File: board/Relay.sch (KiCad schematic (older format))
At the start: 18 parts, among them K1 JS1-12V-F, K2 JS1-12V-F, K3 JS1-12V-F, K4 JS1-12V-F, U4 ULN2003A

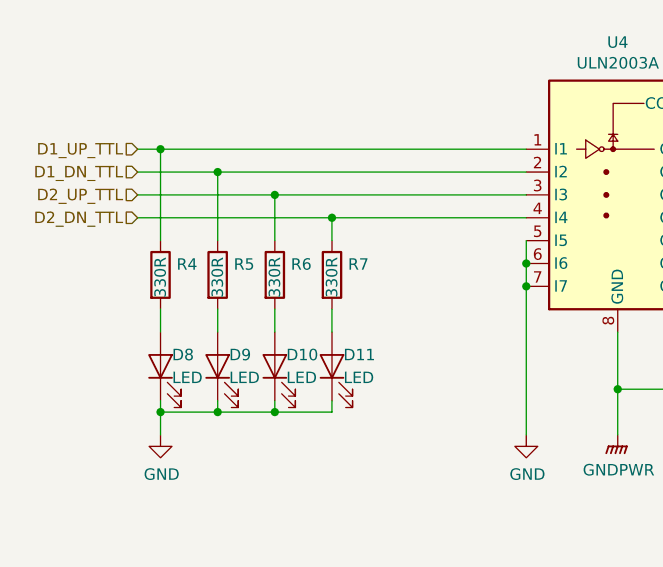
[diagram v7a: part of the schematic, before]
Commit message: Update all footprints to KiCad 5 paths
* All footprints updated.
* 3D models for the relays seem to be missing from KiCad, however, so I
  have a copy in my personal library. Mostly cosmetic.
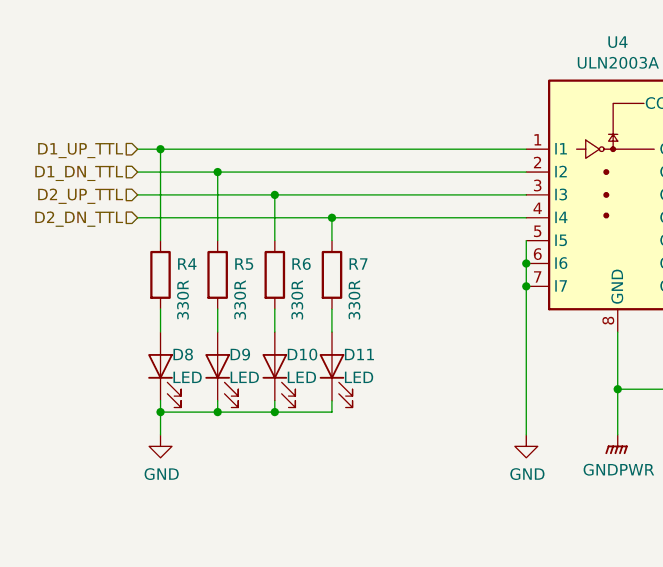
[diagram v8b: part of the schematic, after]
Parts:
- C13: footprint Capacitors_THT:C_Disc_D5.0mm_W2.5mm_P2.50mm -> Capacitor_THT:C_Disc_D5.0mm_W2.5mm_P2.50mm
- D1, D2, D3, D4: footprint Diodes_THT:D_DO-41_SOD81_P10.16mm_Horizontal -> Diode_THT:D_DO-41_SOD81_P10.16mm_Horizontal
- D10, D11, D8, D9: footprint LEDs:LED_D3.0mm -> LED_THT:LED_D3.0mm
- K1, K2, K3, K4: footprint Relays_THT:Relay_SPDT_SANYOU_SRD_Series_Form_C -> Relay_THT:Relay_SPDT_SANYOU_SRD_Series_Form_C
- R4, R5, R6, R7: footprint Resistors_THT:R_Axial_DIN0207_L6.3mm_D2.5mm_P10.16mm_Horizontal -> Resistor_THT:R_Axial_DIN0207_L6.3mm_D2.5mm_P10.16mm_Horizontal
- U4: footprint Housings_DIP:DIP-16_W7.62mm_LongPads -> Package_DIP:DIP-16_W7.62mm_LongPads
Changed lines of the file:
@@
 F 0 "U4" H 3150 3367 50  0000 C CNN
 F 1 "ULN2003A" H 3150 3276 50  0000 C CNN
-F 2 "Housings_DIP:DIP-16_W7.62mm_LongPads" H 3200 2150 50  0001 L CNN
+F 2 "Package_DIP:DIP-16_W7.62mm_LongPads" H 3200 2150 50  0001 L CNN
 F 3 "http://www.ti.com/lit/ds/symlink/uln2003a.pdf" H 3250 2500 50  0001 C CNN
 	1    3150 2700
@@
 F 0 "K1" H 6880 2096 50  0000 L CNN
 F 1 "JS1-12V-F" H 6880 2005 50  0000 L CNN
-F 2 "Relays_THT:Relay_SPDT_SANYOU_SRD_Series_Form_C" H 6900 2000 50  0001 L CNN
+F 2 "Relay_THT:Relay_SPDT_SANYOU_SRD_Series_Form_C" H 6900 2000 50  0001 L CNN
 F 3 "https://www3.panasonic.biz/ac/cdn/e/control/relay/power/catalog/mech_eng_js.pdf" H 6450 2050 50  0001 C CNN
 	1    6450 2050
@@
 F 0 "K2" H 6880 3046 50  0000 L CNN
 F 1 "JS1-12V-F" H 6880 2955 50  0000 L CNN
-F 2 "Relays_THT:Relay_SPDT_SANYOU_SRD_Series_Form_C" H 6900 2950 50  0001 L CNN
+F 2 "Relay_THT:Relay_SPDT_SANYOU_SRD_Series_Form_C" H 6900 2950 50  0001 L CNN
 F 3 "https://www3.panasonic.biz/ac/cdn/e/control/relay/power/catalog/mech_eng_js.pdf" H 6450 3000 50  0001 C CNN
 	1    6450 3000
@@
 F 0 "K3" H 6880 4046 50  0000 L CNN
 F 1 "JS1-12V-F" H 6880 3955 50  0000 L CNN
-F 2 "Relays_THT:Relay_SPDT_SANYOU_SRD_Series_Form_C" H 6900 3950 50  0001 L CNN
+F 2 "Relay_THT:Relay_SPDT_SANYOU_SRD_Series_Form_C" H 6900 3950 50  0001 L CNN
 F 3 "https://www3.panasonic.biz/ac/cdn/e/control/relay/power/catalog/mech_eng_js.pdf" H 6450 4000 50  0001 C CNN
 	1    6450 4000
@@
 F 0 "K4" H 6880 5096 50  0000 L CNN
 F 1 "JS1-12V-F" H 6880 5005 50  0000 L CNN
-F 2 "Relays_THT:Relay_SPDT_SANYOU_SRD_Series_Form_C" H 6900 5000 50  0001 L CNN
+F 2 "Relay_THT:Relay_SPDT_SANYOU_SRD_Series_Form_C" H 6900 5000 50  0001 L CNN
 F 3 "https://www3.panasonic.biz/ac/cdn/e/control/relay/power/catalog/mech_eng_js.pdf" H 6450 5050 50  0001 C CNN
 	1    6450 5050
@@
 F 0 "D1" V 5604 2129 50  0000 L CNN
 F 1 "1N4004" V 5695 2129 50  0000 L CNN
-F 2 "Diodes_THT:D_DO-41_SOD81_P10.16mm_Horizontal" H 5650 1875 50  0001 C CNN
+F 2 "Diode_THT:D_DO-41_SOD81_P10.16mm_Horizontal" H 5650 1875 50  0001 C CNN
 F 3 "http://www.vishay.com/docs/88503/1n4001.pdf" H 5650 2050 50  0001 C CNN
 	1    5650 2050
@@
 F 0 "D2" V 5604 3029 50  0000 L CNN
 F 1 "1N4004" V 5695 3029 50  0000 L CNN
-F 2 "Diodes_THT:D_DO-41_SOD81_P10.16mm_Horizontal" H 5650 2775 50  0001 C CNN
+F 2 "Diode_THT:D_DO-41_SOD81_P10.16mm_Horizontal" H 5650 2775 50  0001 C CNN
 F 3 "http://www.vishay.com/docs/88503/1n4001.pdf" H 5650 2950 50  0001 C CNN
 	1    5650 2950
@@
 F 0 "D3" V 5604 4079 50  0000 L CNN
 F 1 "1N4004" V 5695 4079 50  0000 L CNN
-F 2 "Diodes_THT:D_DO-41_SOD81_P10.16mm_Horizontal" H 5650 3825 50  0001 C CNN
+F 2 "Diode_THT:D_DO-41_SOD81_P10.16mm_Horizontal" H 5650 3825 50  0001 C CNN
 F 3 "http://www.vishay.com/docs/88503/1n4001.pdf" H 5650 4000 50  0001 C CNN
 	1    5650 4000
@@
 F 0 "D4" V 5604 5129 50  0000 L CNN
 F 1 "1N4004" V 5695 5129 50  0000 L CNN
-F 2 "Diodes_THT:D_DO-41_SOD81_P10.16mm_Horizontal" H 5650 4875 50  0001 C CNN
+F 2 "Diode_THT:D_DO-41_SOD81_P10.16mm_Horizontal" H 5650 4875 50  0001 C CNN
 F 3 "http://www.vishay.com/docs/88503/1n4001.pdf" H 5650 5050 50  0001 C CNN
 	1    5650 5050
@@
 P 1900 3050
 F 0 "R7" H 1970 3096 50  0000 L CNN
-F 1 "330R" V 1900 2950 50  0000 L CNN
-F 2 "Resistors_THT:R_Axial_DIN0207_L6.3mm_D2.5mm_P10.16mm_Horizontal" V 1830 3050 50  0001 C CNN
+F 1 "330R" V 2000 2850 50  0000 L CNN
+F 2 "Resistor_THT:R_Axial_DIN0207_L6.3mm_D2.5mm_P10.16mm_Horizontal" V 1830 3050 50  0001 C CNN
 F 3 "~" H 1900 3050 50  0001 C CNN
 	1    1900 3050
@@
 P 1650 3050
 F 0 "R6" H 1720 3096 50  0000 L CNN
-F 1 "330R" V 1650 2950 50  0000 L CNN
-F 2 "Resistors_THT:R_Axial_DIN0207_L6.3mm_D2.5mm_P10.16mm_Horizontal" V 1580 3050 50  0001 C CNN
+F 1 "330R" V 1750 2850 50  0000 L CNN
+F 2 "Resistor_THT:R_Axial_DIN0207_L6.3mm_D2.5mm_P10.16mm_Horizontal" V 1580 3050 50  0001 C CNN
 F 3 "~" H 1650 3050 50  0001 C CNN
 	1    1650 3050
@@
 P 1400 3050
 F 0 "R5" H 1470 3096 50  0000 L CNN
-F 1 "330R" V 1400 2950 50  0000 L CNN
-F 2 "Resistors_THT:R_Axial_DIN0207_L6.3mm_D2.5mm_P10.16mm_Horizontal" V 1330 3050 50  0001 C CNN
+F 1 "330R" V 1500 2850 50  0000 L CNN
+F 2 "Resistor_THT:R_Axial_DIN0207_L6.3mm_D2.5mm_P10.16mm_Horizontal" V 1330 3050 50  0001 C CNN
 F 3 "~" H 1400 3050 50  0001 C CNN
 	1    1400 3050
@@
 F 0 "D8" V 1200 3400 50  0000 R CNN
 F 1 "LED" V 1100 3400 50  0000 R CNN
-F 2 "LEDs:LED_D3.0mm" H 1150 3450 50  0001 C CNN
+F 2 "LED_THT:LED_D3.0mm" H 1150 3450 50  0001 C CNN
 F 3 "~" H 1150 3450 50  0001 C CNN
 	1    1150 3450
@@
 F 0 "D9" V 1450 3400 50  0000 R CNN
 F 1 "LED" V 1350 3400 50  0000 R CNN
-F 2 "LEDs:LED_D3.0mm" H 1400 3450 50  0001 C CNN
+F 2 "LED_THT:LED_D3.0mm" H 1400 3450 50  0001 C CNN
 F 3 "~" H 1400 3450 50  0001 C CNN
 	1    1400 3450
@@
 F 0 "D10" V 1700 3400 50  0000 R CNN
 F 1 "LED" V 1600 3400 50  0000 R CNN
-F 2 "LEDs:LED_D3.0mm" H 1650 3450 50  0001 C CNN
+F 2 "LED_THT:LED_D3.0mm" H 1650 3450 50  0001 C CNN
 F 3 "~" H 1650 3450 50  0001 C CNN
 	1    1650 3450
@@
 F 0 "D11" V 1950 3400 50  0000 R CNN
 F 1 "LED" V 1850 3400 50  0000 R CNN
-F 2 "LEDs:LED_D3.0mm" H 1900 3450 50  0001 C CNN
+F 2 "LED_THT:LED_D3.0mm" H 1900 3450 50  0001 C CNN
 F 3 "~" H 1900 3450 50  0001 C CNN
 	1    1900 3450
@@
 P 1150 3050
 F 0 "R4" H 1220 3096 50  0000 L CNN
-F 1 "330R" V 1150 2950 50  0000 L CNN
-F 2 "Resistors_THT:R_Axial_DIN0207_L6.3mm_D2.5mm_P10.16mm_Horizontal" V 1080 3050 50  0001 C CNN
+F 1 "330R" V 1250 2850 50  0000 L CNN
+F 2 "Resistor_THT:R_Axial_DIN0207_L6.3mm_D2.5mm_P10.16mm_Horizontal" V 1080 3050 50  0001 C CNN
 F 3 "~" H 1150 3050 50  0001 C CNN
 	1    1150 3050
@@
 F 0 "C13" H 3815 3396 50  0000 L CNN
 F 1 "0.1uF" H 3815 3305 50  0000 L CNN
-F 2 "Capacitors_THT:C_Disc_D5.0mm_W2.5mm_P2.50mm" H 3738 3200 50  0001 C CNN
+F 2 "Capacitor_THT:C_Disc_D5.0mm_W2.5mm_P2.50mm" H 3738 3200 50  0001 C CNN
 F 3 "~" H 3700 3350 50  0001 C CNN
 	1    3700 3350
